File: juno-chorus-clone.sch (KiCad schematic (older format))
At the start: 168 parts, among them P1 15VAC_IN, P2 AUDIO_IN, P3 AUDIO_OUT_1, P4 AUDIO_OUT_2, Q1 2SC1815, Q10 2SC1815, Q11 2SA1015, Q12 2SA1015, Q13 2SC1815, Q14 2SA1015, Q15 2SA1015, Q16 2SK30, Q17 2SK30, Q18 2SA1015, Q19 2SA1015, Q2 2SC1815, Q3 2SA1015, Q4 2SA1015, Q5 2SC1815, Q6 2SC1815, Q7 2SA1015, Q8 2SA1015, Q9 2SC1815, SW1 SW_PUSH, U1 TL082, U10 TL082, U2 LM7815CT, U3 LM7915CT, U4 TL082, U5 MN3009, U6 MN3101, U7 MN3009, U8 MN3101, U9 TL082

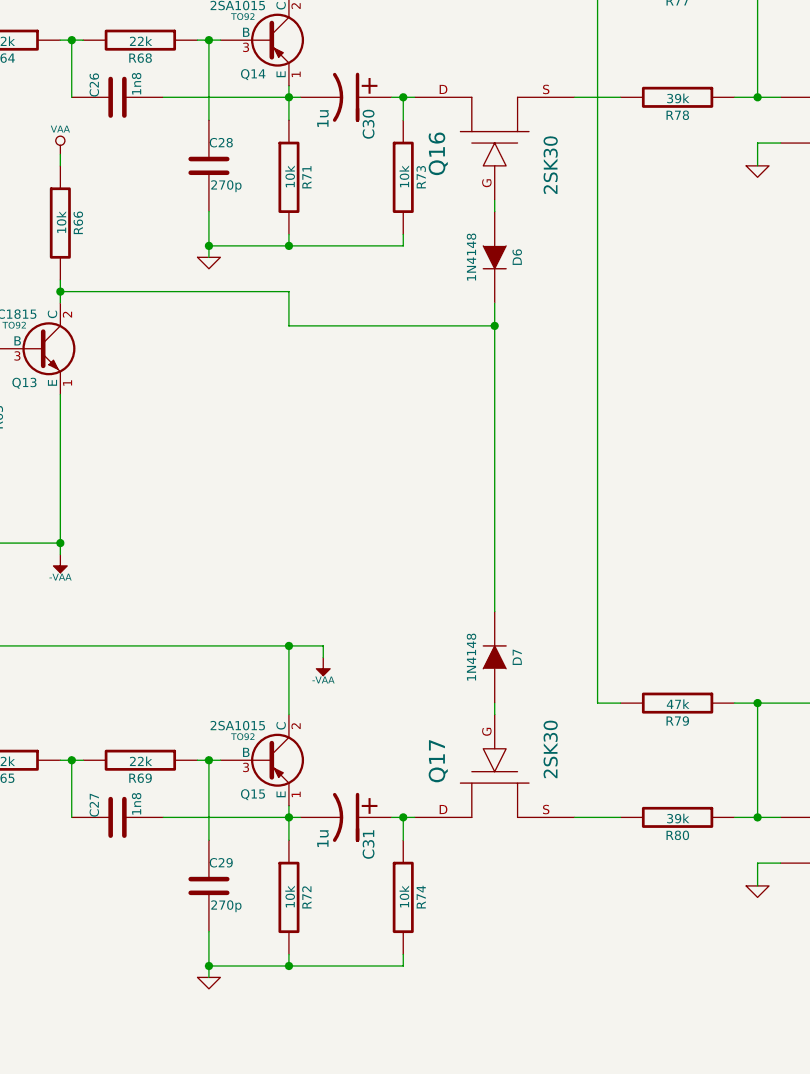
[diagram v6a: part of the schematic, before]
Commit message: sch: fixing wrong res values in BBDs output stages
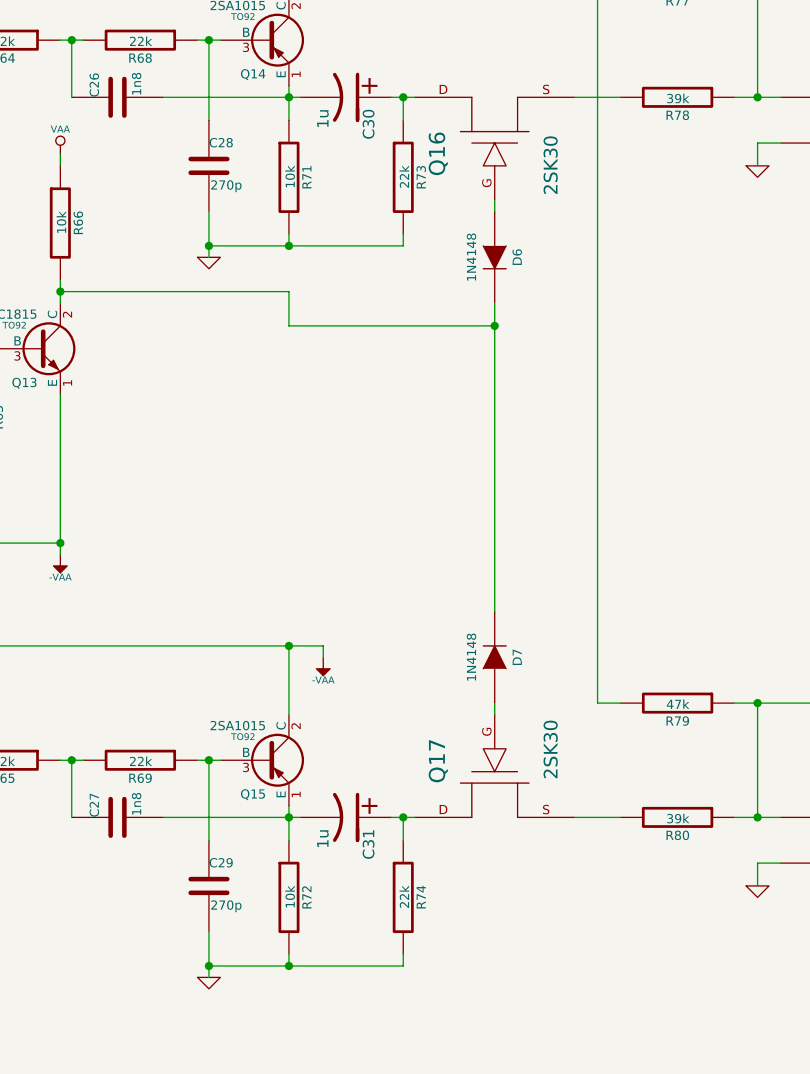
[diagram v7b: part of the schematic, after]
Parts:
- R73, R74: value 10k -> 22k
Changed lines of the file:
@@
 Title "Roland Juno-60 chorus board clone"
 Date "4 may 2014"
-Rev "2"
+Rev "3"
 Comp "GliGli's DIY"
 Comment1 ""
@@
 P 12200 3950
 F 0 "R73" V 12280 3950 40  0000 C CNN
-F 1 "10k" V 12207 3951 40  0000 C CNN
+F 1 "22k" V 12207 3951 40  0000 C CNN
 F 2 "~" V 12130 3950 30  0000 C CNN
 F 3 "~" H 12200 3950 30  0000 C CNN
@@
 P 12200 7100
 F 0 "R74" V 12280 7100 40  0000 C CNN
-F 1 "10k" V 12207 7101 40  0000 C CNN
+F 1 "22k" V 12207 7101 40  0000 C CNN
 F 2 "~" V 12130 7100 30  0000 C CNN
 F 3 "~" H 12200 7100 30  0000 C CNN

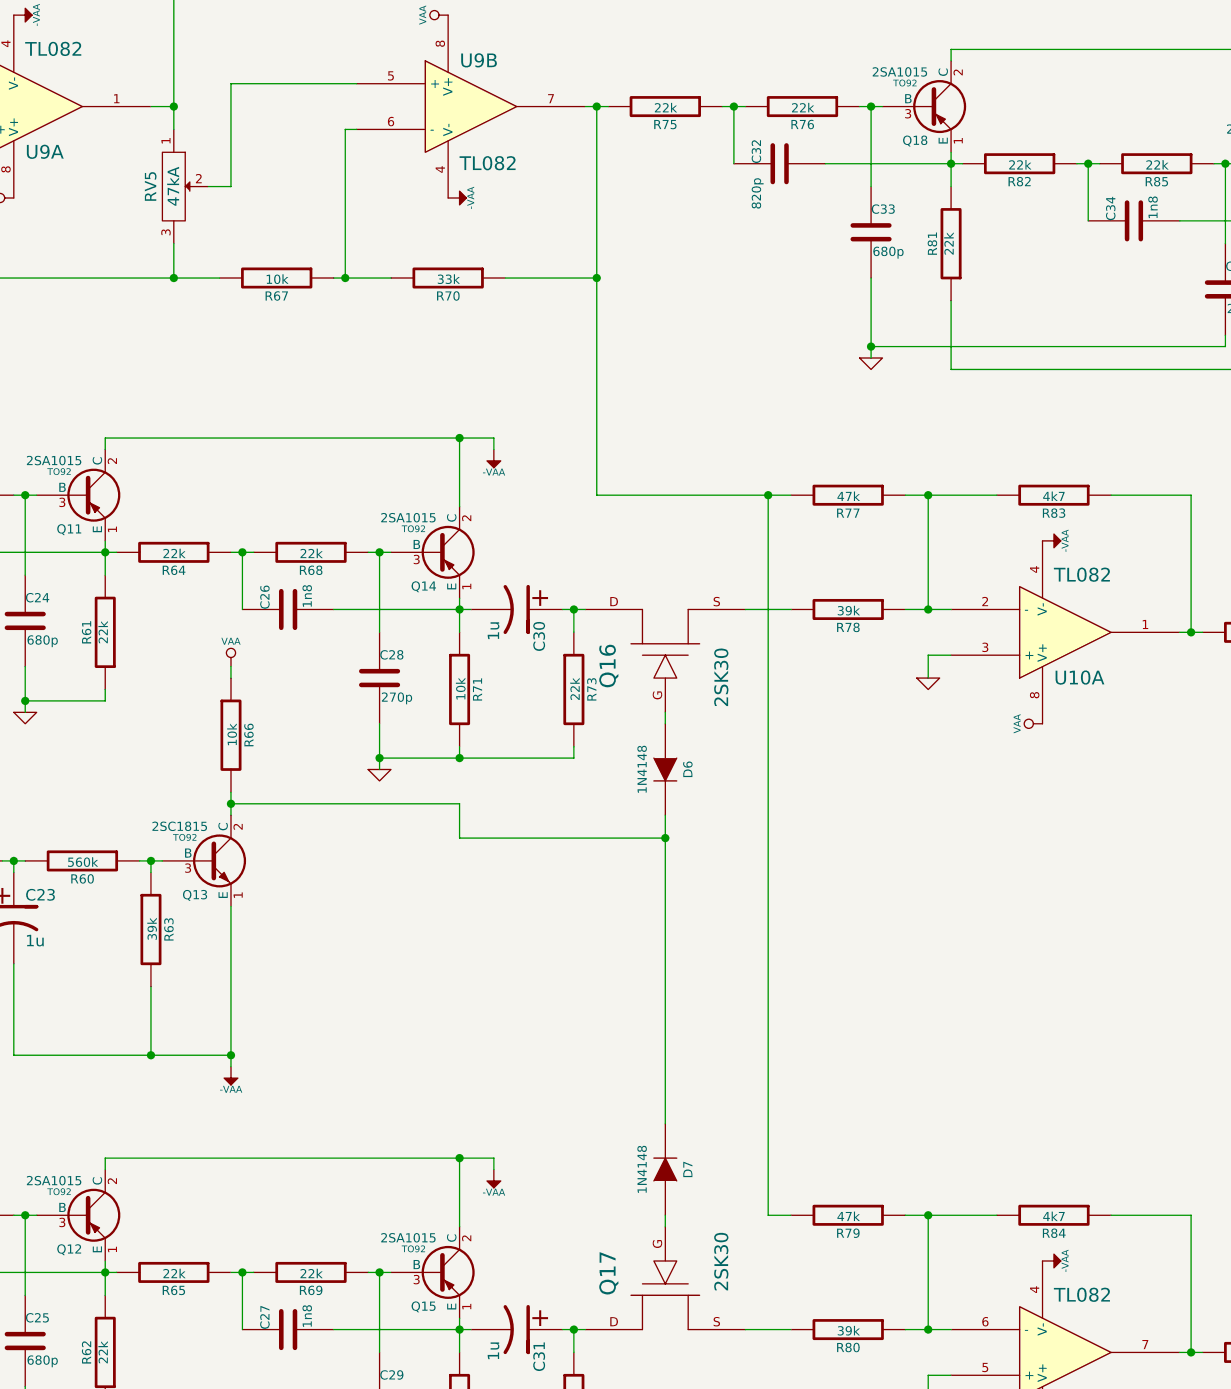
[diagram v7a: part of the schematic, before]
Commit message: sch: output level / input gain pot fixes
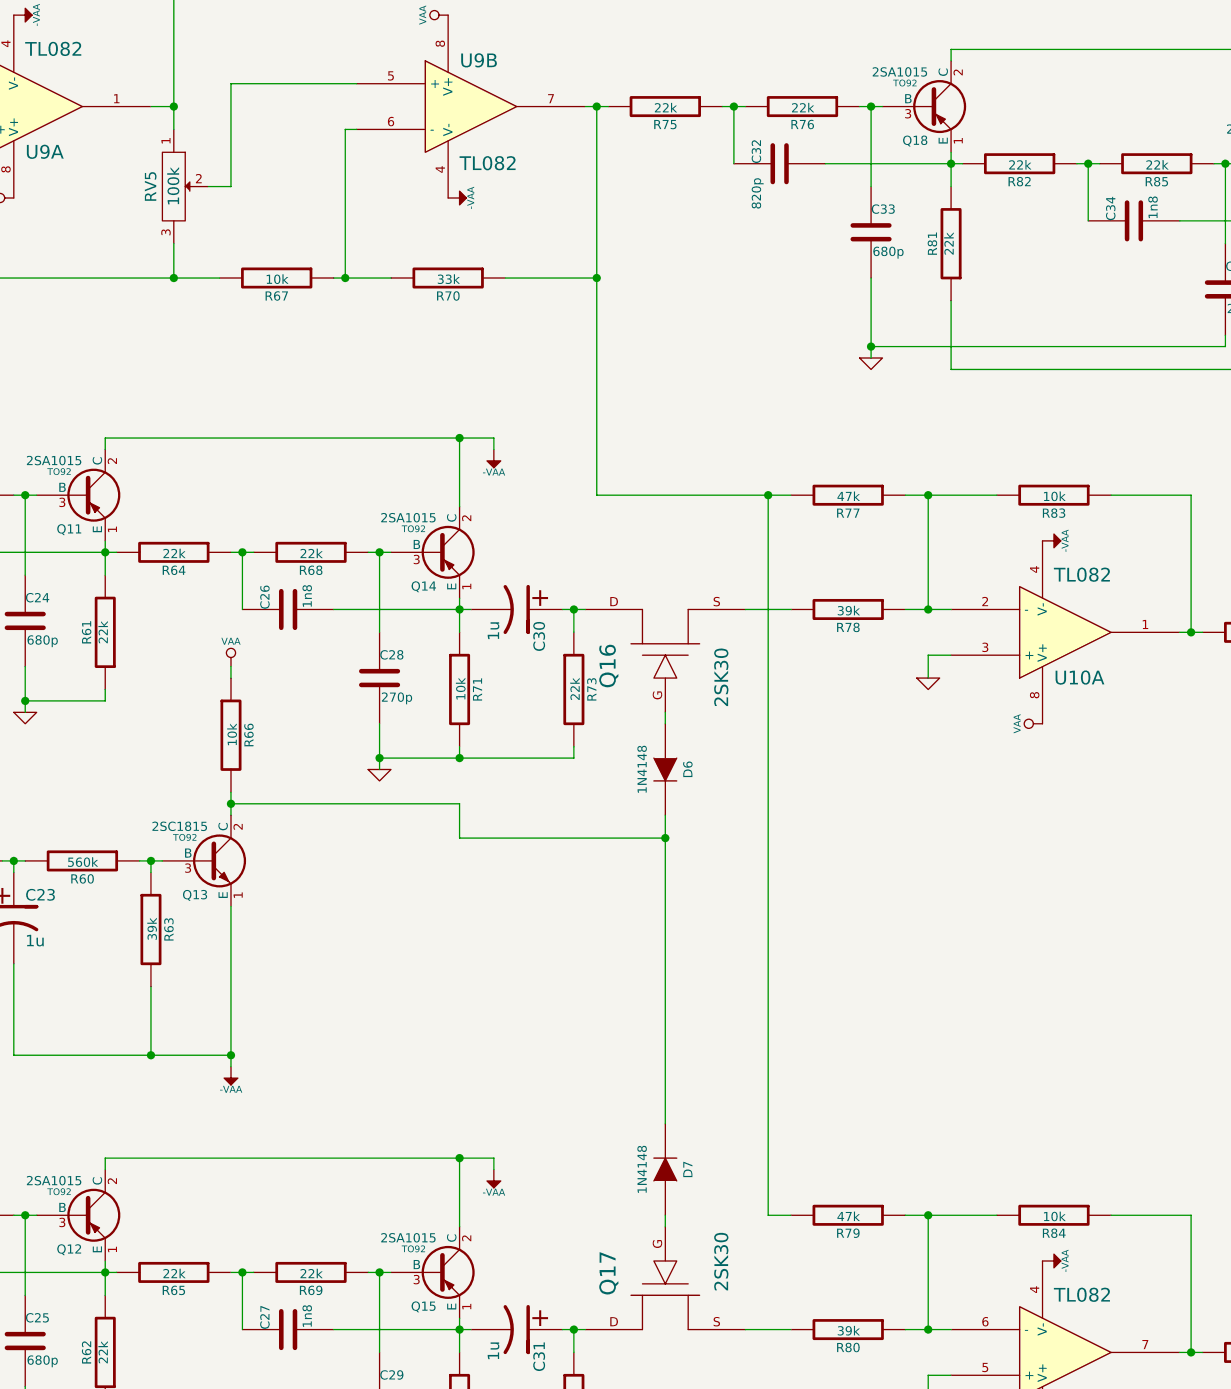
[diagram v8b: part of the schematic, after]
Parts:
- R83, R84: value 4k7 -> 10k
- RV5: value 47kA -> 100k
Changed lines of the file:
@@
 Sheet 1 1
 Title "Roland Juno-60 chorus board clone"
-Date "4 may 2014"
-Rev "3"
+Date "7 may 2014"
+Rev "4"
 Comp "GliGli's DIY"
 Comment1 ""
@@
 P 10450 1750
 F 0 "RV5" H 10450 1650 50  0000 C CNN
-F 1 "47kA" H 10450 1750 50  0000 C CNN
+F 1 "100k" H 10450 1750 50  0000 C CNN
 F 2 "~" H 10450 1750 60  0000 C CNN
 F 3 "~" H 10450 1750 60  0000 C CNN
@@
 P 14300 3100
 F 0 "R83" V 14380 3100 40  0000 C CNN
-F 1 "4k7" V 14307 3101 40  0000 C CNN
+F 1 "10k" V 14307 3101 40  0000 C CNN
 F 2 "~" V 14230 3100 30  0000 C CNN
 F 3 "~" H 14300 3100 30  0000 C CNN
@@
 P 14300 6250
 F 0 "R84" V 14380 6250 40  0000 C CNN
-F 1 "4k7" V 14307 6251 40  0000 C CNN
+F 1 "10k" V 14307 6251 40  0000 C CNN
 F 2 "~" V 14230 6250 30  0000 C CNN
 F 3 "~" H 14300 6250 30  0000 C CNN
